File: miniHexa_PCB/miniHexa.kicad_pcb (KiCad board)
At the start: 4 copper layers, 94 x 65.9 mm, 82 parts, among them J1 FR_L, J2 12v DC, J3 FR_R, J4 MID_L, J5 MID_R, J6 BK_L, J7 BK_R, Q1 BC807, SW1 SW_Push, U1 STM32F401RETx, U2 SN74LVC1G125DBV, U3 RT8289GSP, U4 BQ25886RGE, U5 SN74LVC1G126DBV, U6 AMS1117-3.3, U7 LSM6DS3, U8 ST67W611M1A6UTR, Y2 25mhz

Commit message: fixed RESET button issue
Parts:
- C1: value 20uF -> 2.2uF
- U7: value LSM6DS3 -> LSM6DSL
- moved R1 6.10 mm to (169.2, 94.7), turned to -90 degrees
- moved C13 2.09 mm to (168.0, 92.5), turned to 180 degrees
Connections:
- C13 pad 1: Net-(U1-NRST) -> GND
- C13 pad 2: GND -> NRST
- R1 pad 1: Net-(R1-Pad1) -> NRST
- SW1 pad 1: Net-(R1-Pad1) -> GND
- SW1 pad 2: Net-(U1-NRST) -> NRST
- U1 pad 46: unconnected-(U1-PA13-Pad46) -> SWDIO
- U1 pad 49: unconnected-(U1-PA14-Pad49) -> SWCLK
- U1 pad 7: Net-(U1-NRST) -> NRST
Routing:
- net NRST: track 0.00 -> 8.68 mm
- net Net-(U1-NRST): track 8.61 -> 0.00 mm
- net +3.3V: track 195.7 -> 197.1 mm
- net GND: track 166.2 -> 166.8 mm

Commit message: updated some power lines
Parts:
- moved R23 2.37 mm to (190.8, 71.8)
- moved C22 0.07 mm to (194.6, 73.8)
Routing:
- net GND: track 166.8 -> 162.0 mm, vias 27 -> 30
- net VIN: track 20.2 -> 16.2 mm
- net Net-(U3-EN): track 4.89 -> 2.95 mm
- net Net-(BT1-+): track 28.0 -> 27.5 mm
- removed copper zone on In2.Cu, net +3.3V

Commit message: tried to make it cleaner
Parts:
- removed R3: 0, Resistor_SMD:R_0603_1608Metric
- added JP1: 0hm, Resistor_SMD:R_0603_1608Metric, F.Cu at (158.8, 81.9)
- moved D3 0.35 mm to (185.2, 82.5)
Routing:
- net +3.3V: track 197.1 -> 195.0 mm
- net GND: track 162.0 -> 163.7 mm
- net Net-(U4-BTST): track 11.5 -> 10.2 mm
- added copper zone on B.Cu, net GND

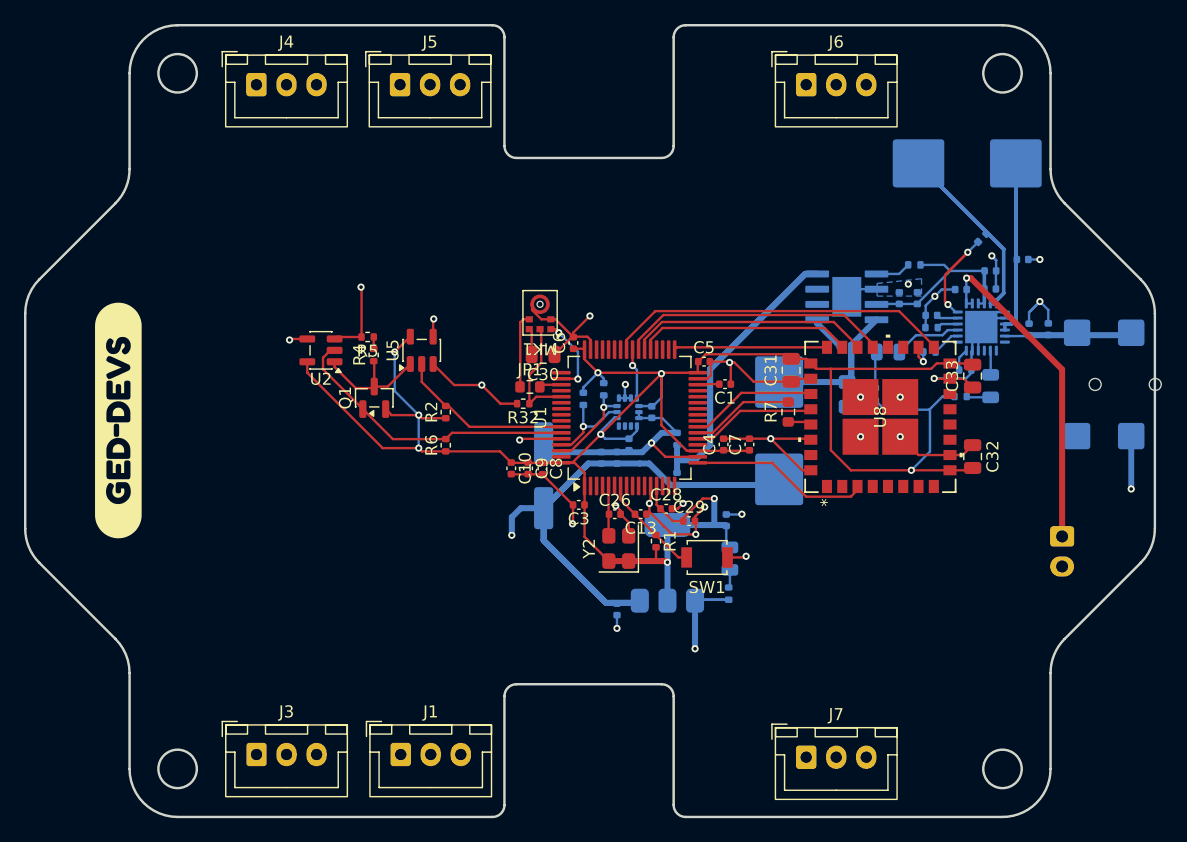
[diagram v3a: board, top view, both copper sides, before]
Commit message: cleaned up; no major DRC violation
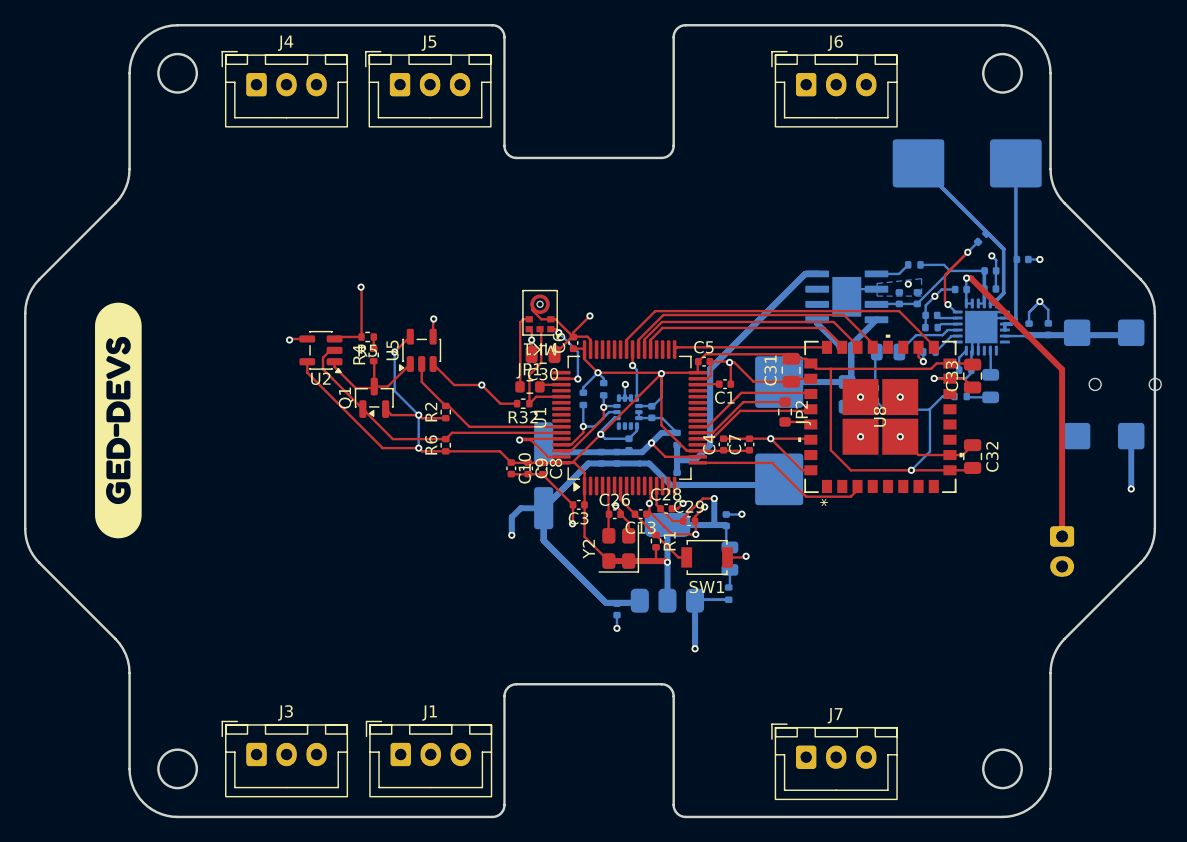
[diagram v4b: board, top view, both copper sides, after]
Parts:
- removed R7: 0, Resistor_SMD:R_0603_1608Metric
- added JP2: 0hm, Resistor_SMD:R_0603_1608Metric, F.Cu at (180.0, 84.0)
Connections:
- net /Power_handler/12V renamed /POWER HANDLER/12V
- JP1 pad 2: MIC_SCK -> Net-(JP1-B)
- U1 pad 51: MIC_SCK -> Net-(JP1-B)
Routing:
- net Net-(C23-Pad2): track 42.1 -> 16.2 mm
- net +3.3V: track 195.0 -> 201.6 mm, vias 9 -> 10
- net GND: track 163.7 -> 167.7 mm
- net MIC_SCK: track 8.07 -> 6.23 mm
- net Net-(JP1-B): track 0.00 -> 1.85 mm

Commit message: changed footprint for pol cap; Need to adjust font size for the silk screen
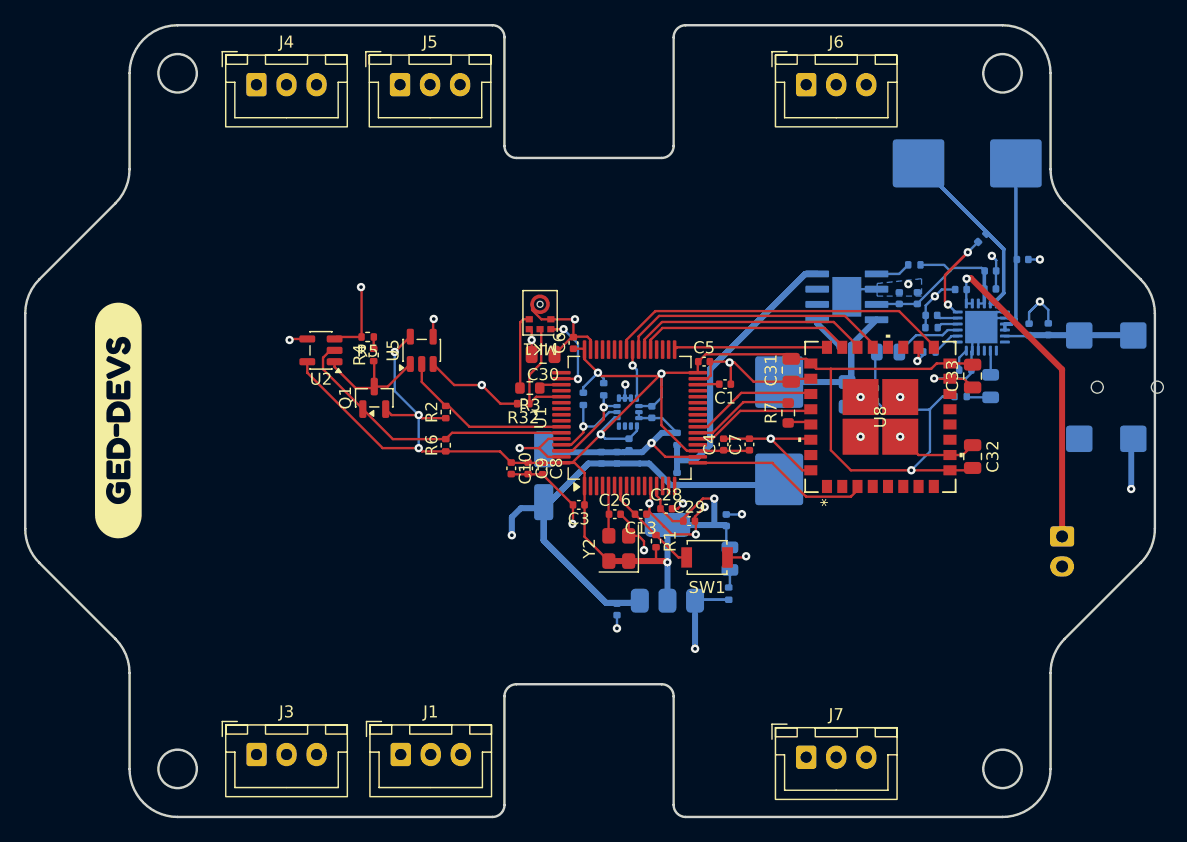
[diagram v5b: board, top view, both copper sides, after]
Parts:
- removed JP1, JP2: 0hm, Resistor_SMD:R_0603_1608Metric
- added R3: 0, Resistor_SMD:R_0603_1608Metric, F.Cu at (158.8, 82.0)
- added R7: 0, Resistor_SMD:R_0603_1608Metric, F.Cu at (180.2, 84.1)
- C19: footprint Capacitor_SMD:CP_Elec_6.3x7.7 -> Capacitor_SMD:CP_Elec_5x5.4
- moved J2 0.29 mm to (207.8, 81.9)
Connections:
- net /POWER HANDLER/12V renamed /Power_handler/12V
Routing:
- net GND: track 167.7 -> 166.2 mm
